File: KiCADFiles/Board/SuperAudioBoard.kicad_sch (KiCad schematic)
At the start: 0 parts

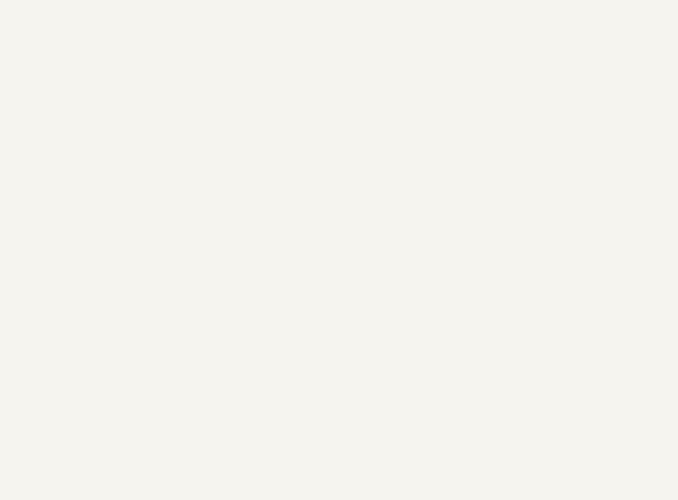
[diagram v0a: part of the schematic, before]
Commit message: finished layout, passed DRC
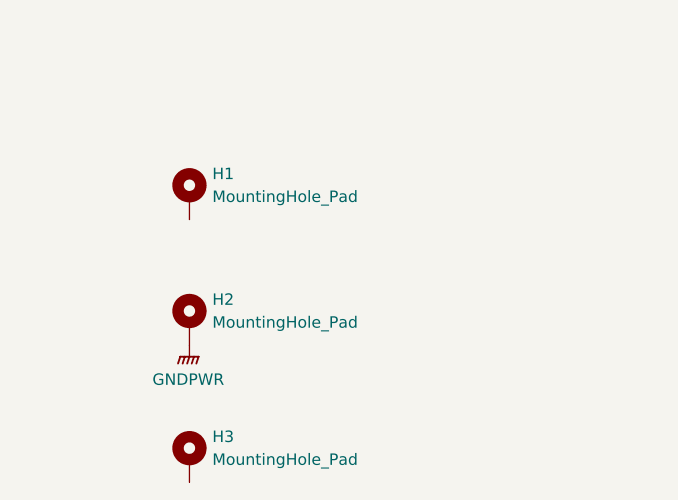
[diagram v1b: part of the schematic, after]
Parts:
- added H1, H2, H3: MountingHole_Pad, MountingHole:MountingHole_3.2mm_M3_DIN965_Pad, symbol Mechanical:MountingHole_Pad
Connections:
- new net GNDPWR: H2.1

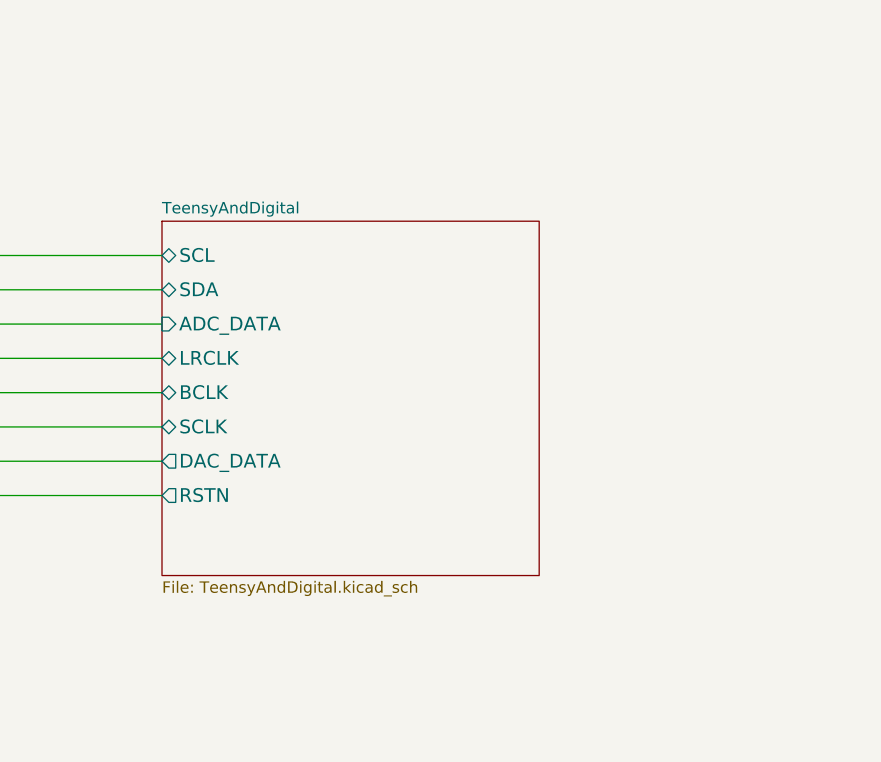
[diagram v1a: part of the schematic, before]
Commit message: added LED driver JST connector
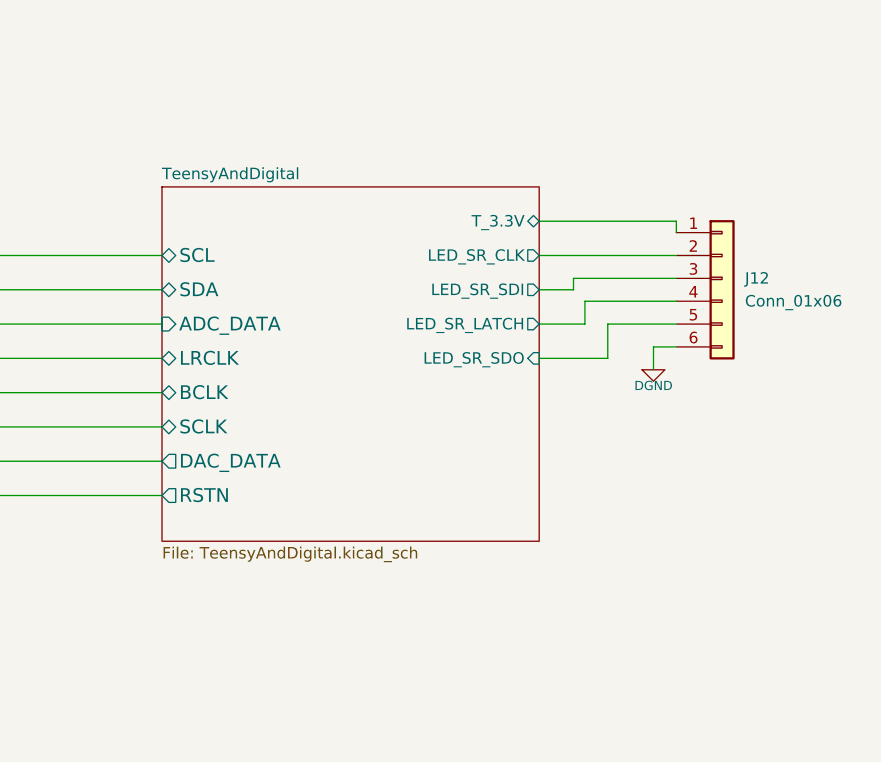
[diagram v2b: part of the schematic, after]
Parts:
- added J12: Conn_01x06, Connector_JST:JST_EH_B6B-EH-A_1x06_P2.50mm_Vertical, symbol Connector_Generic:Conn_01x06
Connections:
- new net DGND: J12.6 (Pin_6)
- new net TeensyAndDigital/LED_SR_CLK: J12.2 (Pin_2)
- new net TeensyAndDigital/LED_SR_LATCH: J12.4 (Pin_4)
- new net TeensyAndDigital/LED_SR_SDI: J12.3 (Pin_3)
- new net TeensyAndDigital/LED_SR_SDO: J12.5 (Pin_5)
- new net TeensyAndDigital/T_3.3V: J12.1 (Pin_1)
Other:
- sheet TeensyAndDigital ports: added LED_SR_CLK, LED_SR_LATCH, LED_SR_SDI, LED_SR_SDO, T_3.3V; removed none
